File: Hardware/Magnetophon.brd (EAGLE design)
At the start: 105 x 19 mm, 22 parts, among them U2 TL072_

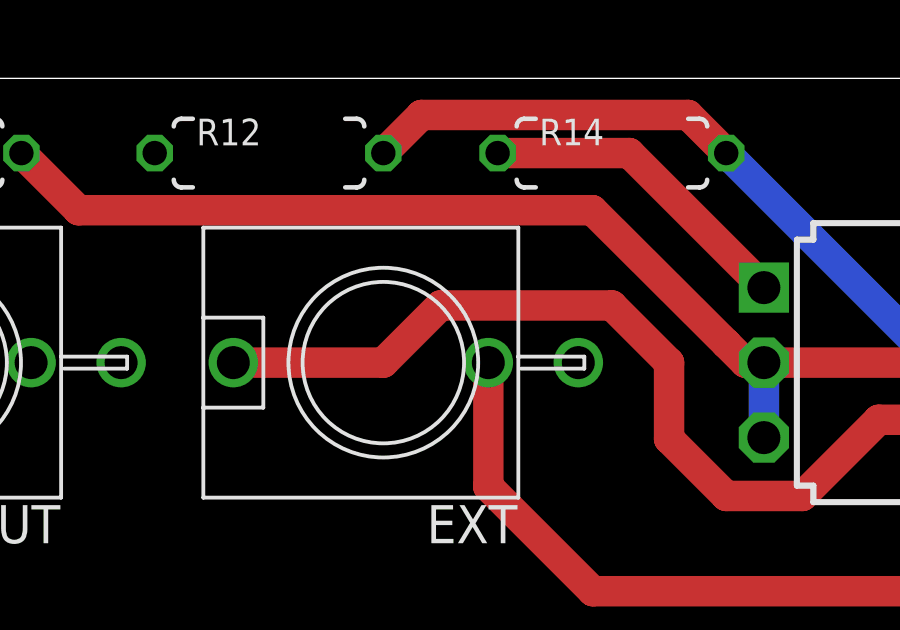
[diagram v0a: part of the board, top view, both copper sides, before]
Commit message: Add via to ground panel artwork
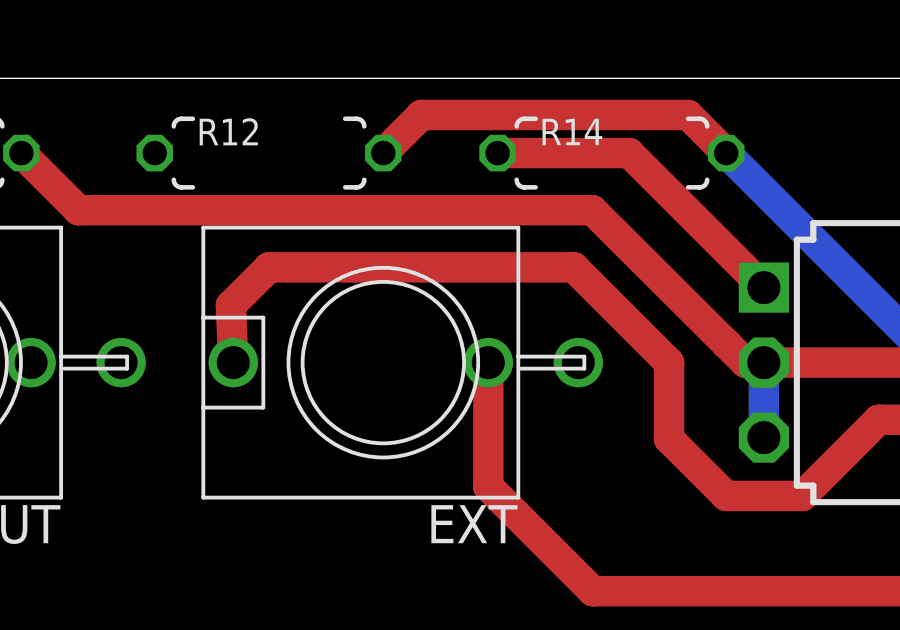
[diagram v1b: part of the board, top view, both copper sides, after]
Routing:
- net N$2: track 44.9 -> 47.2 mm
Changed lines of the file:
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@@
 <?xml version="1.0" encoding="utf-8"?>
 <!DOCTYPE eagle SYSTEM "eagle.dtd">
-<eagle version="7.2.0">
+<eagle version="7.4.0">
 <drawing>
 <settings>
@@
 By Tom Whitwell October 2015
 PCB Prototype 1 CC-BY-SA</text>
-<text x="32.512" y="11.557" size="0.762" layer="22" font="vector" distance="40" rot="MR0">Inspired by: Laurie Anderson, Nam June Paik,
+<text x="32.512" y="11.557" size="0.762" layer="30" font="vector" ratio="12" distance="40" rot="MR0">Inspired by: Laurie Anderson, Nam June Paik,
 Brian Eno, Stockhausen, Yoko Ono, Steve Reich,
 Sender &amp; Subotnik, Terry Riley,  Halim El-Dabh,
@@
 <vertex x="48.60798125" y="1.234440625"/>
 </polygon>
+<rectangle x1="65.405" y1="13.97" x2="85.725" y2="15.875" layer="30"/>
 </plain>
 <attributes>
@@
 <contactref element="U2" pad="3"/>
 <contactref element="EXT" pad="P$1_TIP"/>
-<wire x1="16.59" y1="9.525" x2="21.59" y2="9.525" width="1.016" layer="1"/>
-<wire x1="21.59" y1="9.525" x2="23.495" y2="11.43" width="1.016" layer="1"/>
-<wire x1="23.495" y1="11.43" x2="29.21" y2="11.43" width="1.016" layer="1"/>
-<wire x1="29.21" y1="11.43" x2="31.115" y2="9.525" width="1.016" layer="1"/>
+<wire x1="16.59" y1="9.525" x2="16.51" y2="11.43" width="1.016" layer="1"/>
+<wire x1="16.51" y1="11.43" x2="17.78" y2="12.7" width="1.016" layer="1"/>
+<wire x1="17.78" y1="12.7" x2="27.94" y2="12.7" width="1.016" layer="1"/>
+<wire x1="27.94" y1="12.7" x2="31.115" y2="9.525" width="1.016" layer="1"/>
 <wire x1="31.115" y1="9.525" x2="31.115" y2="6.985" width="1.016" layer="1"/>
 <wire x1="31.115" y1="6.985" x2="33.02" y2="5.08" width="1.016" layer="1"/>
